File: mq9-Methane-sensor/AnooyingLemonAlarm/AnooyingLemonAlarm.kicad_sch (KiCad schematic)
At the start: 12 parts, among them SW1 SW_MEC_5E, SW2 SW_MEC_5E, SW3 SW_MEC_5E, SW4 SW_MEC_5E, U2 DS3231M

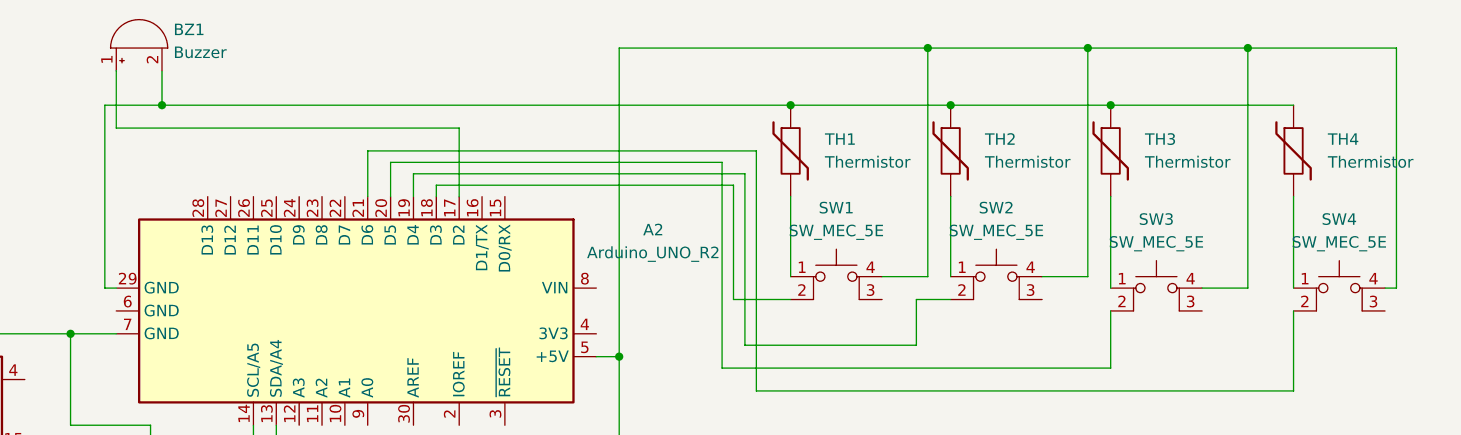
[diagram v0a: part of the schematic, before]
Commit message: mq-9 and Nic4 fix
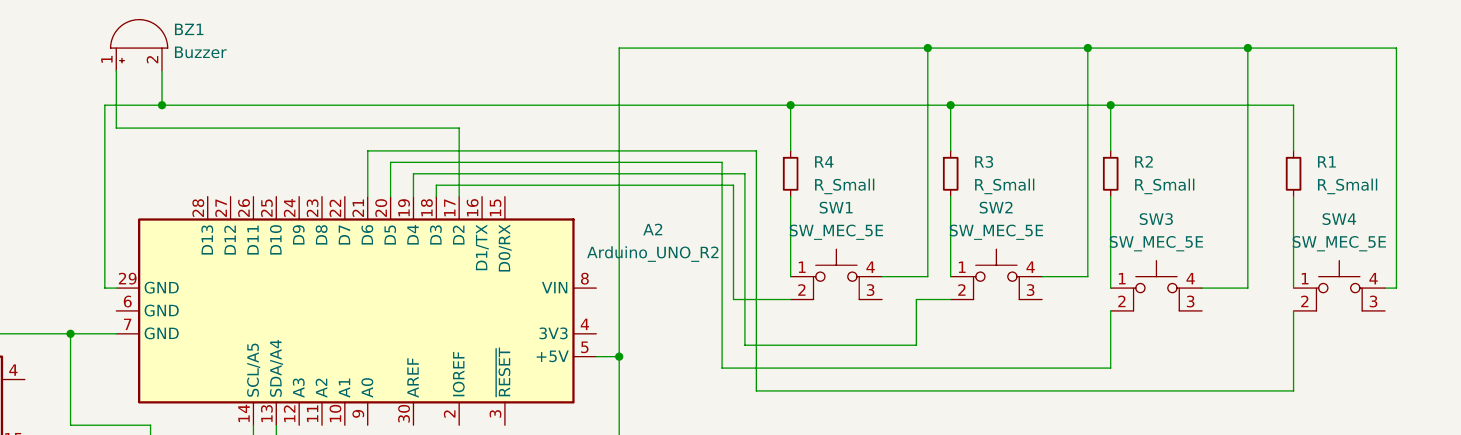
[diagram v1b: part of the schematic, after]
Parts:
- removed TH1, TH2, TH3, TH4: Thermistor, symbol Device:Thermistor
- added R1, R2, R3, R4: R_Small, symbol Device:R_Small
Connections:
- net at A2.29 (GND), BZ1.2 (+): now also R1.1, R2.1, R3.1, R4.1
- net at SW2.1: now also R3.2
- net at SW1.1: now also R4.2
- net at SW4.1: now also R1.2
- net at SW3.1: now also R2.2
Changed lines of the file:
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@@
     (comment 1 "Group 4 Project")
   )
+  (junction (at 170.18 55.88) (diameter 0) (color 0 0 0 1)
+  )
   (junction (at 185.42 49.53) (diameter 0) (color 255 0 0 1)
   )
-  (junction (at 170.18 55.88) (diameter 0) (color 0 0 0 1)
-  )
   (junction (at 151.13 83.82) (diameter 0) (color 255 0 9 1)
   )
@@
   (junction (at 205.74 55.88) (diameter 0) (color 0 0 0 1)
   )
+  (junction (at 187.96 55.88) (diameter 0) (color 0 0 0 1)
+  )
   (junction (at 100.33 55.88) (diameter 0) (color 0 0 0 1)
   )
   (junction (at 203.2 49.53) (diameter 0) (color 255 0 0 1)
-  )
-  (junction (at 187.96 55.88) (diameter 0) (color 0 0 0 1)
   )
   (junction (at 91.44 96.52) (diameter 0) (color 0 0 0 0)
@@
     (stroke (width 0) (type default) (color 255 0 9 1))
   )
-  (wire (pts (xy 170.18 55.88) (xy 187.96 55.88))
-    (stroke (width 0) (type default) (color 0 0 0 1))
-  )
   (wire (pts (xy 151.13 49.53) (xy 185.42 49.53))
     (stroke (width 0) (type default) (color 255 0 9 1))
@@
     (stroke (width 0) (type default))
   )
-  (wire (pts (xy 187.96 55.88) (xy 205.74 55.88))
+  (wire (pts (xy 100.33 55.88) (xy 170.18 55.88))
     (stroke (width 0) (type default) (color 0 0 0 1))
   )
@@
     (stroke (width 0) (type default) (color 255 0 0 1))
   )
+  (wire (pts (xy 170.18 55.88) (xy 170.18 60.96))
+    (stroke (width 0) (type default) (color 0 0 0 1))
+  )
   (wire (pts (xy 151.13 83.82) (xy 151.13 49.53))
     (stroke (width 0) (type default) (color 255 0 9 1))
@@
     (stroke (width 0) (type default))
   )
-  (wire (pts (xy 205.74 55.88) (xy 226.06 55.88))
+  (wire (pts (xy 170.18 55.88) (xy 187.96 55.88))
     (stroke (width 0) (type default) (color 0 0 0 1))
   )
@@
   (wire (pts (xy 220.98 76.2) (xy 220.98 49.53))
     (stroke (width 0) (type default) (color 255 0 0 1))
-  )
-  (wire (pts (xy 170.18 55.88) (xy 100.33 55.88))
-    (stroke (width 0) (type default) (color 0 0 0 1))
   )
   (wire (pts (xy 90.17 91.44) (xy 90.17 81.28))
@@
     (stroke (width 0) (type default))
   )
+  (wire (pts (xy 205.74 55.88) (xy 205.74 60.96))
+    (stroke (width 0) (type default) (color 0 0 0 1))
+  )
   (wire (pts (xy 184.15 82.55) (xy 165.1 82.55))
     (stroke (width 0) (type default))
@@
   (wire (pts (xy 185.42 74.93) (xy 185.42 49.53))
     (stroke (width 0) (type default) (color 255 0 0 1))
+  )
+  (wire (pts (xy 205.74 55.88) (xy 226.06 55.88))
+    (stroke (width 0) (type default) (color 0 0 0 1))
+  )
+  (wire (pts (xy 187.96 55.88) (xy 205.74 55.88))
+    (stroke (width 0) (type default) (color 0 0 0 1))
+  )
+  (wire (pts (xy 187.96 55.88) (xy 187.96 60.96))
+    (stroke (width 0) (type default) (color 0 0 0 1))
   )
   (wire (pts (xy 99.06 129.54) (xy 99.06 91.44))
@@
     (stroke (width 0) (type default))
   )
+  (wire (pts (xy 226.06 55.88) (xy 226.06 60.96))
+    (stroke (width 0) (type default) (color 0 0 0 1))
+  )
   (wire (pts (xy 87.63 93.98) (xy 113.03 93.98))
     (stroke (width 0) (type default))
@@
   (wire (pts (xy 163.83 77.47) (xy 163.83 64.77))
     (stroke (width 0) (type default))
+  )
+  (symbol (lib_id "Device:R_Small") (at 205.74 63.5 0) (unit 1)
+    (in_bom yes) (on_board yes) (dnp no) (fields_autoplaced)
+    (property "Reference" "R2" (at 208.28 62.23 0)
+      (effects (font (size 1.27 1.27)) (justify left))
+    )
+    (property "Value" "R_Small" (at 208.28 64.77 0)
+      (effects (font (size 1.27 1.27)) (justify left))
+    )
+    (property "Footprint" "" (at 205.74 63.5 0)
+      (effects (font (size 1.27 1.27)) hide)
+    )
+    (property "Datasheet" "~" (at 205.74 63.5 0)
+      (effects (font (size 1.27 1.27)) hide)
+    )
+    (pin "1")
+    (pin "2")
+    (instances
+      (project "AnooyingLemonAlarm"
+        (path "/6482a796-0b5a-4553-bc94-95c04af4dcb1"
+          (reference "R2") (unit 1)
+        )
+      )
+    )
+  )
+  (symbol (lib_id "Device:R_Small") (at 187.96 63.5 0) (unit 1)
+    (in_bom yes) (on_board yes) (dnp no) (fields_autoplaced)
+    (property "Reference" "R3" (at 190.5 62.23 0)
+      (effects (font (size 1.27 1.27)) (justify left))
+    )
+    (property "Value" "R_Small" (at 190.5 64.77 0)
+      (effects (font (size 1.27 1.27)) (justify left))
+    )
+    (property "Footprint" "" (at 187.96 63.5 0)
+      (effects (font (size 1.27 1.27)) hide)
+    )
+    (property "Datasheet" "~" (at 187.96 63.5 0)
+      (effects (font (size 1.27 1.27)) hide)
+    )
+    (pin "1")
+    (pin "2")
+    (instances
+      (project "AnooyingLemonAlarm"
+        (path "/6482a796-0b5a-4553-bc94-95c04af4dcb1"
+          (reference "R3") (unit 1)
+        )
+      )
+    )
   )
   (symbol (lib_id "OLED-128x64:OLED128X64") (at 92.71 132.08 0) (unit 1)
@@
         (path "/6482a796-0b5a-4553-bc94-95c04af4dcb1"
           (reference "U1") (unit 1)
-        )
-      )
-    )
-  )
-  (symbol (lib_id "Device:Thermistor") (at 187.96 60.96 0) (unit 1)
-    (in_bom yes) (on_board yes) (dnp no) (fields_autoplaced)
-    (property "Reference" "TH2" (at 191.77 59.69 0)
-      (effects (font (size 1.27 1.27)) (justify left))
-    )
-    (property "Value" "Thermistor" (at 191.77 62.23 0)
-      (effects (font (size 1.27 1.27)) (justify left))
-    )
-    (property "Footprint" "" (at 187.96 60.96 0)
-      (effects (font (size 1.27 1.27)) hide)
-    )
-    (property "Datasheet" "~" (at 187.96 60.96 0)
-      (effects (font (size 1.27 1.27)) hide)
-    )
-    (pin "1")
-    (pin "2")
-    (instances
-      (project "AnooyingLemonAlarm"
-        (path "/6482a796-0b5a-4553-bc94-95c04af4dcb1"
-          (reference "TH2") (unit 1)
         )
       )
@@
     )
   )
-  (symbol (lib_id "Device:Thermistor") (at 226.06 60.96 0) (unit 1)
-    (in_bom yes) (on_board yes) (dnp no) (fields_autoplaced)
-    (property "Reference" "TH4" (at 229.87 59.69 0)
-      (effects (font (size 1.27 1.27)) (justify left))
-    )
-    (property "Value" "Thermistor" (at 229.87 62.23 0)
-      (effects (font (size 1.27 1.27)) (justify left))
-    )
-    (property "Footprint" "" (at 226.06 60.96 0)
-      (effects (font (size 1.27 1.27)) hide)
-    )
-    (property "Datasheet" "~" (at 226.06 60.96 0)
-      (effects (font (size 1.27 1.27)) hide)
-    )
-    (pin "1")
-    (pin "2")
-    (instances
-      (project "AnooyingLemonAlarm"
-        (path "/6482a796-0b5a-4553-bc94-95c04af4dcb1"
-          (reference "TH4") (unit 1)
-        )
-      )
-    )
-  )
   (symbol (lib_id "Timer_RTC:DS3231M") (at 72.39 91.44 180) (unit 1)
     (in_bom yes) (on_board yes) (dnp no)
@@
     )
   )
-  (symbol (lib_id "Device:Thermistor") (at 205.74 60.96 0) (unit 1)
-    (in_bom yes) (on_board yes) (dnp no) (fields_autoplaced)
-    (property "Reference" "TH3" (at 209.55 59.69 0)
-      (effects (font (size 1.27 1.27)) (justify left))
-    )
-    (property "Value" "Thermistor" (at 209.55 62.23 0)
-      (effects (font (size 1.27 1.27)) (justify left))
-    )
-    (property "Footprint" "" (at 205.74 60.96 0)
-      (effects (font (size 1.27 1.27)) hide)
-    )
-    (property "Datasheet" "~" (at 205.74 60.96 0)
-      (effects (font (size 1.27 1.27)) hide)
-    )
-    (pin "1")
-    (pin "2")
-    (instances
-      (project "AnooyingLemonAlarm"
-        (path "/6482a796-0b5a-4553-bc94-95c04af4dcb1"
-          (reference "TH3") (unit 1)
+  (symbol (lib_id "Device:R_Small") (at 170.18 63.5 0) (unit 1)
+    (in_bom yes) (on_board yes) (dnp no) (fields_autoplaced)
+    (property "Reference" "R4" (at 172.72 62.23 0)
+      (effects (font (size 1.27 1.27)) (justify left))
+    )
+    (property "Value" "R_Small" (at 172.72 64.77 0)
+      (effects (font (size 1.27 1.27)) (justify left))
+    )
+    (property "Footprint" "" (at 170.18 63.5 0)
+      (effects (font (size 1.27 1.27)) hide)
+    )
+    (property "Datasheet" "~" (at 170.18 63.5 0)
+      (effects (font (size 1.27 1.27)) hide)
+    )
+    (pin "1")
+    (pin "2")
+    (instances
+      (project "AnooyingLemonAlarm"
+        (path "/6482a796-0b5a-4553-bc94-95c04af4dcb1"
+          (reference "R4") (unit 1)
         )
       )
@@
         (path "/6482a796-0b5a-4553-bc94-95c04af4dcb1"
           (reference "SW3") (unit 1)
-        )
-      )
-    )
-  )
-  (symbol (lib_id "Device:Thermistor") (at 170.18 60.96 0) (unit 1)
-    (in_bom yes) (on_board yes) (dnp no) (fields_autoplaced)
-    (property "Reference" "TH1" (at 173.99 59.69 0)
-      (effects (font (size 1.27 1.27)) (justify left))
-    )
-    (property "Value" "Thermistor" (at 173.99 62.23 0)
-      (effects (font (size 1.27 1.27)) (justify left))
-    )
-    (property "Footprint" "" (at 170.18 60.96 0)
-      (effects (font (size 1.27 1.27)) hide)
-    )
-    (property "Datasheet" "~" (at 170.18 60.96 0)
-      (effects (font (size 1.27 1.27)) hide)
-    )
-    (pin "1")
-    (pin "2")
-    (instances
-      (project "AnooyingLemonAlarm"
-        (path "/6482a796-0b5a-4553-bc94-95c04af4dcb1"
-          (reference "TH1") (unit 1)
         )
       )
@@
         )
       )
+    )
+  )
+  (symbol (lib_id "Device:R_Small") (at 226.06 63.5 0) (unit 1)
+    (in_bom yes) (on_board yes) (dnp no) (fields_autoplaced)
+    (property "Reference" "R1" (at 228.6 62.23 0)
+      (effects (font (size 1.27 1.27)) (justify left))
+    )
+    (property "Value" "R_Small" (at 228.6 64.77 0)
+      (effects (font (size 1.27 1.27)) (justify left))
+    )
+    (property "Footprint" "" (at 226.06 63.5 0)
+      (effects (font (size 1.27 1.27)) hide)
+    )
+    (property "Datasheet" "~" (at 226.06 63.5 0)
+      (effects (font (size 1.27 1.27)) hide)
+    )
+    (pin "1")
+    (pin "2")
+    (instances
+      (project "AnooyingLemonAlarm"
+        (path "/6482a796-0b5a-4553-bc94-95c04af4dcb1"
+          (reference "R1") (unit 1)
+        )
+      )
